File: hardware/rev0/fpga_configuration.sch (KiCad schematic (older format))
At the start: 25 parts, among them IC1 ECP5-BGA256, J5 Conn_ARM_JTAG_SWD_10, J6 Conn_ARM_JTAG_SWD_10, U6 ATSAMD21G18A-AUT, U7 W25Q32JVSS

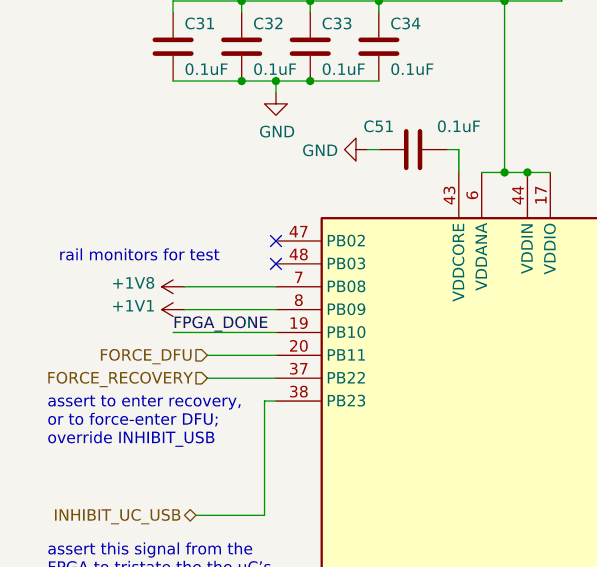
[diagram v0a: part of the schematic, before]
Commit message: Switch to 3V3 for RAM, remove 1V8 rail
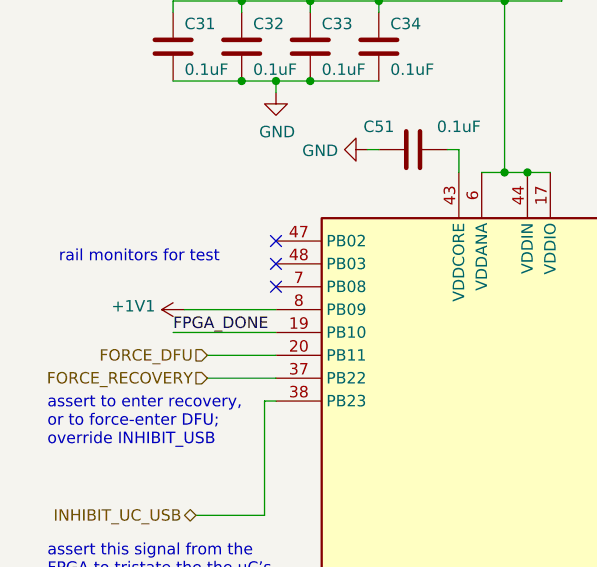
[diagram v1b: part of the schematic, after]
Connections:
- net +1V8: no longer names the net of U6.7 (PB08)
- no-connect marks 16 -> 17
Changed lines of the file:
@@
 FPGA_CONFIG_CLK
-$Comp
-L power:+1V8 #PWR039
-U 1 1 5DC07181
-P 1150 2350
-F 0 "#PWR039" H 1150 2200 50  0001 C CNN
-F 1 "+1V8" V 1165 2478 50  0000 L CNN
-F 2 "" H 1150 2350 50  0001 C CNN
-F 3 "" H 1150 2350 50  0001 C CNN
-	1    1150 2350
-	0    -1   -1   0
-$EndComp
-Wire Wire Line
-	1150 2350 1550 2350
 $Comp
 L power:+1V1 #PWR040
@@
 Text HLabel 4150 3650 2    50   Output ~ 0
 DEBUG_SPI_CS
+NoConn ~ 1550 2350
 $EndSCHEMATC

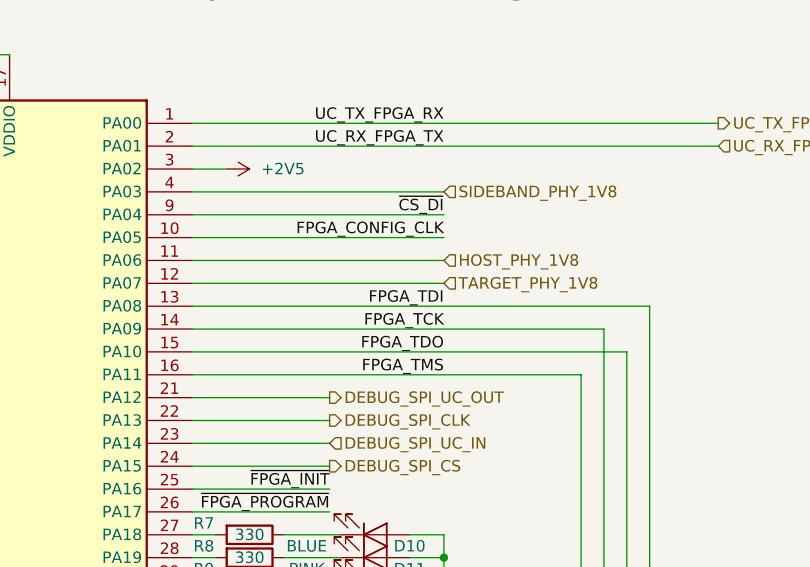
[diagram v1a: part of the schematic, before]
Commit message: Route/NC remaining target signals, ERC & schematic cleanup
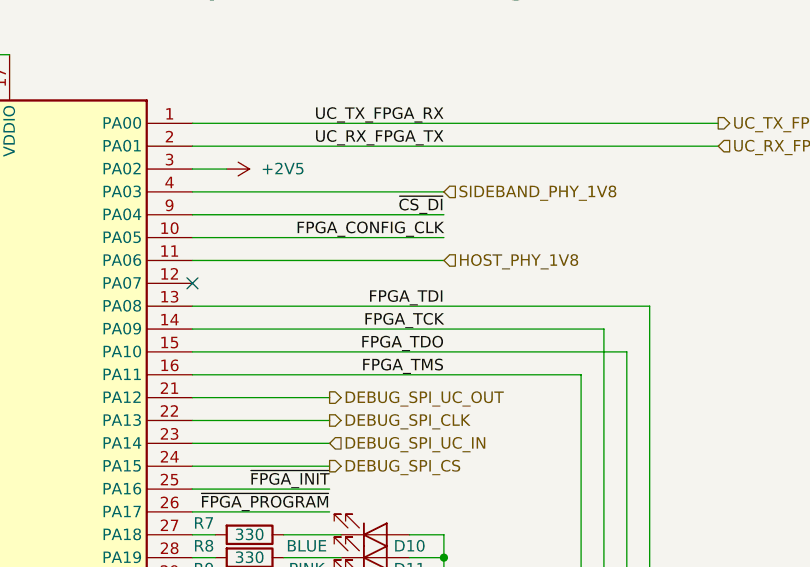
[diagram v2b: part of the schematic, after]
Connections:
- net TARGET_PHY_1V8: no longer names the net of U6.12 (PA07)
- no-connect marks 17 -> 18
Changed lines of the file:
@@
 Wire Wire Line
 	3550 2750 4650 2750
-Wire Wire Line
-	3550 2850 4650 2850
 NoConn ~ 3550 4750
 NoConn ~ 3550 4850
@@
 Text HLabel 4650 2750 2    50   Input ~ 0
 HOST_PHY_1V8
-Text HLabel 4650 2850 2    50   Input ~ 0
-TARGET_PHY_1V8
 NoConn ~ 9450 2900
 NoConn ~ 9450 3000
@@
 DEBUG_SPI_CS
 NoConn ~ 1550 2350
+NoConn ~ 3550 2850
 $EndSCHEMATC

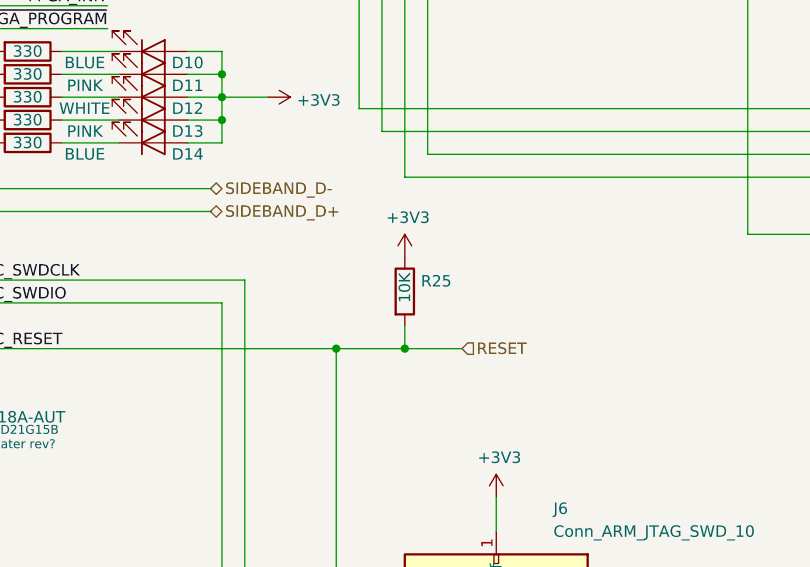
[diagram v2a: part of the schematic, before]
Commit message: Tidy up component values
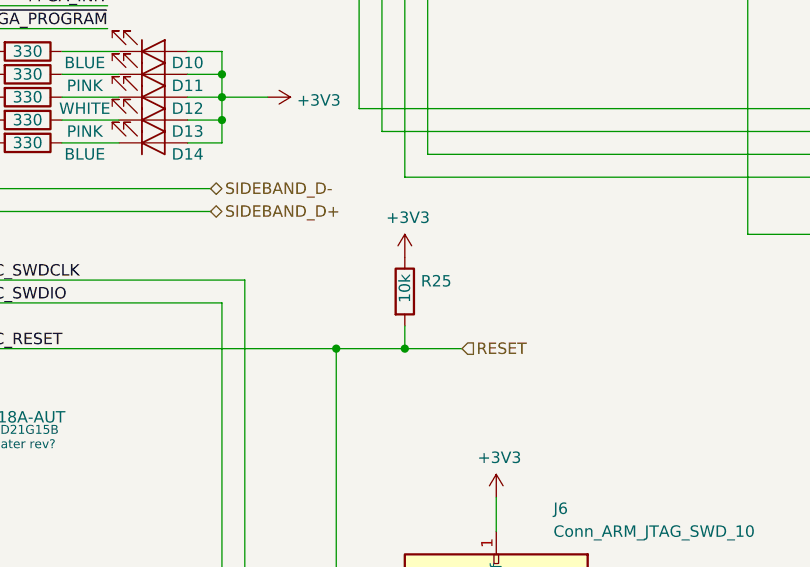
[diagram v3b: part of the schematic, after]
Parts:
- R25: value 10K -> 10k
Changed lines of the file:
@@
 P 5450 5000
 F 0 "R25" H 5520 5045 50  0000 L CNN
-F 1 "10K" V 5450 4950 50  0000 L CNN
+F 1 "10k" V 5450 4950 50  0000 L CNN
 F 2 "Resistor_SMD:R_0402_1005Metric" V 5380 5000 50  0001 C CNN
 F 3 "~" H 5450 5000 50  0001 C CNN

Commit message: Pick part numbers for BOM
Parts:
- C31, C32, C33, C34, C35, C51: Manufacturer_Part_Number (none) -> LMF105B7104KVHF
- D10, D14: Manufacturer_Part_Number (none) -> KB DELPS2.12-QHRI-24-Z555-10-S
- D12: Manufacturer_Part_Number (none) -> KW DELPS2.RA-QISI-FK0PM0-U515
- J5, J6: Manufacturer_Part_Number (none) -> SHF-105-01-L-D-TH
- R10, R11, R7, R8, R9: Manufacturer_Part_Number (none) -> CRCW0402330RFKEDC
- R12, R13, R14, R25: Manufacturer_Part_Number (none) -> CRCW040210K0FKEDC
- U6: Manufacturer_Part_Number (none) -> ATSAMD21G18A-AUT
- U7: Manufacturer_Part_Number (none) -> W25Q32JVSS
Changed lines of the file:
@@
 F 2 "Capacitor_SMD:C_0402_1005Metric" H 1438 1150 50  0001 C CNN
 F 3 "~" H 1400 1300 50  0001 C CNN
+F 4 "LMF105B7104KVHF" H 1400 1300 50  0001 C CNN "Manufacturer_Part_Number"
 	1    1400 1300
 	1    0    0    -1
@@
 F 2 "Capacitor_SMD:C_0402_1005Metric" H 1738 1150 50  0001 C CNN
 F 3 "~" H 1700 1300 50  0001 C CNN
+F 4 "LMF105B7104KVHF" H 1700 1300 50  0001 C CNN "Manufacturer_Part_Number"
 	1    1700 1300
 	1    0    0    -1
@@
 F 2 "Capacitor_SMD:C_0402_1005Metric" H 2038 1150 50  0001 C CNN
 F 3 "~" H 2000 1300 50  0001 C CNN
+F 4 "LMF105B7104KVHF" H 2000 1300 50  0001 C CNN "Manufacturer_Part_Number"
 	1    2000 1300
 	1    0    0    -1
@@
 F 2 "Capacitor_SMD:C_0402_1005Metric" H 1138 1150 50  0001 C CNN
 F 3 "~" H 1100 1300 50  0001 C CNN
+F 4 "LMF105B7104KVHF" H 1100 1300 50  0001 C CNN "Manufacturer_Part_Number"
 	1    1100 1300
 	1    0    0    -1
@@
 F 2 "Package_SO:SOIC-8_5.23x5.23mm_P1.27mm" H 7850 1350 50  0001 C CNN
 F 3 "http://www.winbond.com/resource-files/w25q32jv%20revg%2003272018%20plus.pdf" H 7850 1350 50  0001 C CNN
+F 4 "W25Q32JVSS" H 7850 1350 50  0001 C CNN "Manufacturer_Part_Number"
 	1    7850 1350
 	1    0    0    -1
@@
 F 2 "Capacitor_SMD:C_0402_1005Metric" H 7138 750 50  0001 C CNN
 F 3 "~" H 7100 900 50  0001 C CNN
+F 4 "LMF105B7104KVHF" H 7100 900 50  0001 C CNN "Manufacturer_Part_Number"
 	1    7100 900
 	0    1    1    0
@@
 F 2 "Resistor_SMD:R_0402_1005Metric" V 8680 4950 50  0001 C CNN
 F 3 "~" H 8750 4950 50  0001 C CNN
+F 4 "CRCW040210K0FKEDC" H 8750 4950 50  0001 C CNN "Manufacturer_Part_Number"
 	1    8750 4950
 	0    1    1    0
@@
 F 2 "Resistor_SMD:R_0402_1005Metric" V 8680 5050 50  0001 C CNN
 F 3 "~" H 8750 5050 50  0001 C CNN
+F 4 "CRCW040210K0FKEDC" H 8750 5050 50  0001 C CNN "Manufacturer_Part_Number"
 	1    8750 5050
 	0    1    1    0
@@
 F 2 "Resistor_SMD:R_0402_1005Metric" V 8680 5150 50  0001 C CNN
 F 3 "~" H 8750 5150 50  0001 C CNN
+F 4 "CRCW040210K0FKEDC" H 8750 5150 50  0001 C CNN "Manufacturer_Part_Number"
 	1    8750 5150
 	0    1    1    0
@@
 F 2 "amalthea:SWD_CONNECTOR_LARGE_BOX" H 5850 6650 50  0001 C CNN
 F 3 "http://infocenter.arm.com/help/topic/com.arm.doc.ddi0314h/DDI0314H_coresight_components_trm.pdf" V 5500 5400 50  0001 C CNN
+F 4 "SHF-105-01-L-D-TH" H 5850 6650 50  0001 C CNN "Manufacturer_Part_Number"
 	1    5850 6650
 	-1   0    0    -1
@@
 F 2 "LED_SMD:LED_0603_1608Metric_Pad1.05x0.95mm_HandSolder" H 4350 4150 50  0001 C CNN
 F 3 "~" H 4350 4150 50  0001 C CNN
+F 4 "KW DELPS2.RA-QISI-FK0PM0-U515" H 4350 4150 50  0001 C CNN "Manufacturer_Part_Number"
 	1    4350 4150
 	1    0    0    1
@@
 F 2 "LED_SMD:LED_0603_1608Metric_Pad1.05x0.95mm_HandSolder" H 4350 4350 50  0001 C CNN
 F 3 "~" H 4350 4350 50  0001 C CNN
+F 4 "KB DELPS2.12-QHRI-24-Z555-10-S" H 4350 4350 50  0001 C CNN "Manufacturer_Part_Number"
 	1    4350 4350
 	1    0    0    1
@@
 F 2 "Resistor_SMD:R_0402_1005Metric" V 3730 3950 50  0001 C CNN
 F 3 "~" H 3800 3950 50  0001 C CNN
+F 4 "CRCW0402330RFKEDC" H 3800 3950 50  0001 C CNN "Manufacturer_Part_Number"
 	1    3800 3950
 	0    1    1    0
@@
 F 2 "Resistor_SMD:R_0402_1005Metric" V 3730 4050 50  0001 C CNN
 F 3 "~" H 3800 4050 50  0001 C CNN
+F 4 "CRCW0402330RFKEDC" H 3800 4050 50  0001 C CNN "Manufacturer_Part_Number"
 	1    3800 4050
 	0    1    1    0
@@
 F 2 "Resistor_SMD:R_0402_1005Metric" V 3730 4150 50  0001 C CNN
 F 3 "~" H 3800 4150 50  0001 C CNN
+F 4 "CRCW0402330RFKEDC" H 3800 4150 50  0001 C CNN "Manufacturer_Part_Number"
 	1    3800 4150
 	0    1    1    0
@@
 F 2 "Resistor_SMD:R_0402_1005Metric" V 3730 4250 50  0001 C CNN
 F 3 "~" H 3800 4250 50  0001 C CNN
+F 4 "CRCW0402330RFKEDC" H 3800 4250 50  0001 C CNN "Manufacturer_Part_Number"
 	1    3800 4250
 	0    1    1    0
@@
 F 2 "Resistor_SMD:R_0402_1005Metric" V 3730 4350 50  0001 C CNN
 F 3 "~" H 3800 4350 50  0001 C CNN
+F 4 "CRCW0402330RFKEDC" H 3800 4350 50  0001 C CNN "Manufacturer_Part_Number"
 	1    3800 4350
 	0    1    1    0
@@
 F 2 "amalthea:SWD_CONNECTOR_LARGE_BOX" H 1750 6650 50  0001 C CNN
 F 3 "http://infocenter.arm.com/help/topic/com.arm.doc.ddi0314h/DDI0314H_coresight_components_trm.pdf" V 1400 5400 50  0001 C CNN
+F 4 "SHF-105-01-L-D-TH" H 1750 6650 50  0001 C CNN "Manufacturer_Part_Number"
 	1    1750 6650
 	-1   0    0    -1
@@
 F 2 "LED_SMD:LED_0603_1608Metric_Pad1.05x0.95mm_HandSolder" H 4350 3950 50  0001 C CNN
 F 3 "~" H 4350 3950 50  0001 C CNN
+F 4 "KB DELPS2.12-QHRI-24-Z555-10-S" H 4350 3950 50  0001 C CNN "Manufacturer_Part_Number"
 	1    4350 3950
 	1    0    0    1
@@
 F 2 "Resistor_SMD:R_0402_1005Metric" V 5380 5000 50  0001 C CNN
 F 3 "~" H 5450 5000 50  0001 C CNN
+F 4 "CRCW040210K0FKEDC" H 5450 5000 50  0001 C CNN "Manufacturer_Part_Number"
 	1    5450 5000
 	1    0    0    -1
@@
 F 2 "Capacitor_SMD:C_0402_1005Metric" H 2188 1600 50  0001 C CNN
 F 3 "~" H 2150 1750 50  0001 C CNN
+F 4 "LMF105B7104KVHF" H 2150 1750 50  0001 C CNN "Manufacturer_Part_Number"
 	1    2150 1750
 	0    1    1    0
@@
 F 2 "Package_QFP:TQFP-48_7x7mm_P0.5mm" H 1600 2000 50  0001 C CNN
 F 3 "http://ww1.microchip.com/downloads/en/DeviceDoc/SAMD21-Family-DataSheet-DS40001882D.pdf" H 2550 4750 50  0001 C CNN
+F 4 "ATSAMD21G18A-AUT" H 2550 3750 50  0001 C CNN "Manufacturer_Part_Number"
 	1    2550 3750
 	-1   0    0    -1

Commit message: Swap JTAG connector part
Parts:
- J5, J6: Manufacturer_Part_Number SHF-105-01-L-D-TH -> FTSH-105-01-F-D-K
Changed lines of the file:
@@
 F 2 "amalthea:SWD_CONNECTOR_LARGE_BOX" H 5850 6650 50  0001 C CNN
 F 3 "http://infocenter.arm.com/help/topic/com.arm.doc.ddi0314h/DDI0314H_coresight_components_trm.pdf" V 5500 5400 50  0001 C CNN
-F 4 "SHF-105-01-L-D-TH" H 5850 6650 50  0001 C CNN "Manufacturer_Part_Number"
+F 4 "FTSH-105-01-F-D-K" H 5850 6650 50  0001 C CNN "Manufacturer_Part_Number"
 	1    5850 6650
 	-1   0    0    -1
@@
 F 2 "amalthea:SWD_CONNECTOR_LARGE_BOX" H 1750 6650 50  0001 C CNN
 F 3 "http://infocenter.arm.com/help/topic/com.arm.doc.ddi0314h/DDI0314H_coresight_components_trm.pdf" V 1400 5400 50  0001 C CNN
-F 4 "SHF-105-01-L-D-TH" H 1750 6650 50  0001 C CNN "Manufacturer_Part_Number"
+F 4 "FTSH-105-01-F-D-K" H 1750 6650 50  0001 C CNN "Manufacturer_Part_Number"
 	1    1750 6650
 	-1   0    0    -1
